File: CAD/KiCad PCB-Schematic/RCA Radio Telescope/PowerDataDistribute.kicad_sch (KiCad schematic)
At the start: 12 parts, among them J7 USB_A, J8 USB_A, Q1 PMOS, U13 MIC23050-SYML-TR

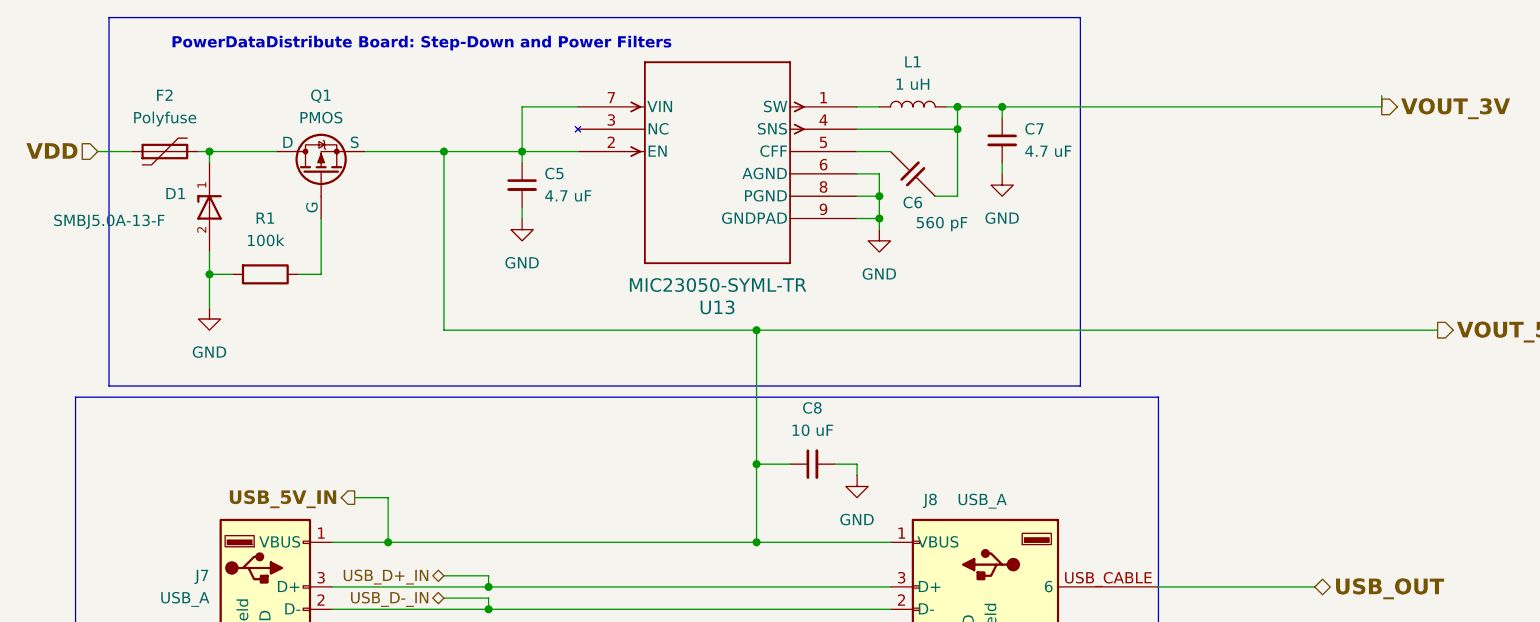
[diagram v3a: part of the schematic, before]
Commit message: Updated PowerDataDistribute schematicto v1.4
- Added components for fuses and PMOS
- Created PCB v1.0
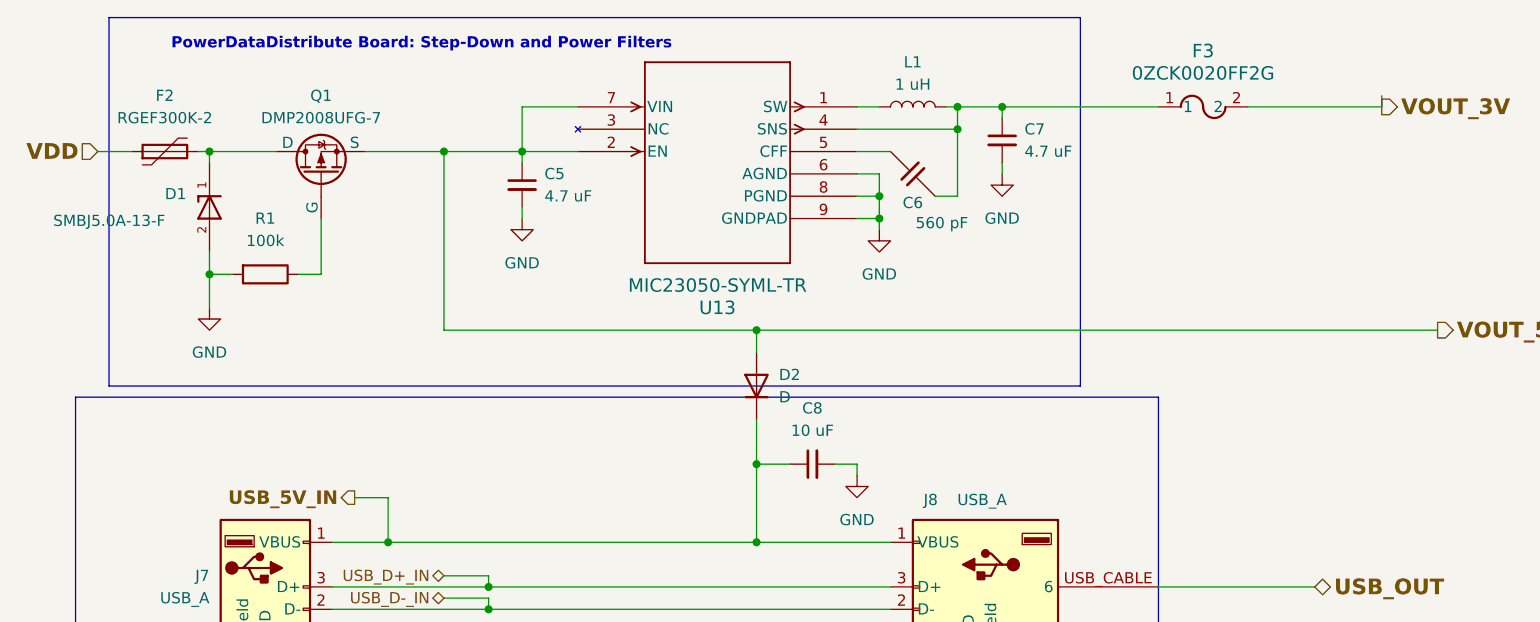
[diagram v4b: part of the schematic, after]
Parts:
- added D2: D, Diode_SMD:D_0805_2012Metric, symbol Device:D
- added F3: 0ZCK0020FF2G, Library:0ZCK_BEL, symbol Radio Telescope:0ZCK0020FF2G
- C5, C6, C7, C8: footprint (none) -> Capacitor_SMD:C_0805_2012Metric
- F2: value Polyfuse -> RGEF300K-2; footprint (none) -> Library:RGEF300K-2
- J7, J8: footprint (none) -> Library:CONN_AU-Y1005-2_ASM
- L1: footprint (none) -> Inductor_SMD:L_0805_2012Metric
- Q1: value PMOS -> DMP2008UFG-7; footprint (none) -> Library:DMP2008UFG-7_DIO
- R1: footprint (none) -> Resistor_SMD:R_0805_2012Metric
- U13: footprint MLF-8_ML_MCH -> Library:MLF-8_ML_MCH
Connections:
- net USB_5V_IN: now also D2.1 (K); no longer C5.1, Q1.3 (S), U13.2 (EN), U13.7 (VIN)
- net VOUT_3V: now also F3.2; no longer C6.1, C7.1, L1.2, U13.4 (SNS)
- new net: C6.1, C7.1, F3.1, L1.2, U13.4 (SNS)
- new net VOUT_5V: C5.1, D2.2 (A), Q1.3 (S), U13.2 (EN), U13.7 (VIN)
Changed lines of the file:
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@@
 	(title_block
 		(title "PowerDataDistribute")
-		(rev "Version 1.3")
+		(date "2025-03-15")
+		(rev "Version 1.4")
 	)
 	(junction
@@
 	)
 	(junction
+		(at 123.19 25.4)
+		(diameter 0)
+		(color 0 0 0 0)
+	)
+	(junction
 		(at 53.34 74.93)
 		(diameter 0)
@@
 	)
 	(junction
-		(at 123.19 25.4)
-		(diameter 0)
-		(color 0 0 0 0)
-	)
-	(junction
 		(at 118.11 27.94)
 		(diameter 0)
@@
 	(wire
 		(pts
+			(xy 95.25 60.96) (xy 95.25 66.04)
+		)
+		(stroke
+			(width 0)
+			(type default)
+		)
+	)
+	(wire
+		(pts
 			(xy 109.22 38.1) (xy 109.22 39.37)
 		)
@@
 	(wire
 		(pts
+			(xy 151.13 25.4) (xy 166.37 25.4)
+		)
+		(stroke
+			(width 0)
+			(type default)
+		)
+	)
+	(wire
+		(pts
 			(xy 104.14 66.04) (xy 106.68 66.04)
 		)
@@
 	(wire
 		(pts
+			(xy 123.19 25.4) (xy 140.97 25.4)
+		)
+		(stroke
+			(width 0)
+			(type default)
+		)
+	)
+	(wire
+		(pts
 			(xy 33.02 44.45) (xy 35.56 44.45)
 		)
@@
 	(wire
 		(pts
-			(xy 123.19 25.4) (xy 166.37 25.4)
-		)
-		(stroke
-			(width 0)
-			(type default)
-		)
-	)
-	(wire
-		(pts
 			(xy 106.68 35.56) (xy 109.22 35.56)
 		)
@@
 	(wire
 		(pts
-			(xy 95.25 50.8) (xy 95.25 66.04)
+			(xy 95.25 50.8) (xy 95.25 53.34)
 		)
 		(stroke
@@
 			)
 		)
-		(property "Value" "Polyfuse"
+		(property "Value" "RGEF300K-2"
 			(at 27.94 26.67 90)
 			(effects
@@
 			)
 		)
-		(property "Footprint" ""
+		(property "Footprint" "Library:RGEF300K-2"
 			(at 33.02 29.21 0)
 			(effects
@@
 			)
 		)
-		(property "Footprint" ""
+		(property "Footprint" "Capacitor_SMD:C_0805_2012Metric"
 			(at 113.03 31.242 0)
 			(effects
@@
 			)
 		)
-		(property "Footprint" "MLF-8_ML_MCH"
+		(property "Footprint" "Library:MLF-8_ML_MCH"
 			(at 72.39 51.308 0)
 			(effects
@@
 			)
 		)
-		(property "Footprint" ""
+		(property "Footprint" "Library:CONN_AU-Y1005-2_ASM"
 			(at 124.46 69.85 0)
 			(effects
@@
 			)
 		)
-		(property "Value" "PMOS"
+		(property "Value" "DMP2008UFG-7"
 			(at 45.72 26.67 90)
 			(effects
@@
 			)
 		)
-		(property "Footprint" ""
+		(property "Footprint" "Library:DMP2008UFG-7_DIO"
 			(at 43.18 27.94 0)
 			(effects
@@
 			)
 		)
-		(property "Footprint" ""
+		(property "Footprint" "Capacitor_SMD:C_0805_2012Metric"
 			(at 68.58 34.29 0)
 			(effects
@@
 				(path "/1630c5ee-b70a-455e-85ba-86a73955b8fd/27e6aa46-cfac-490f-80c1-5c0f7cb6c2e8"
 					(reference "C5")
+					(unit 1)
+				)
+			)
+		)
+	)
+	(symbol
+		(lib_id "Device:D")
+		(at 95.25 57.15 90)
+		(unit 1)
+		(exclude_from_sim no)
+		(in_bom yes)
+		(on_board yes)
+		(dnp no)
+		(fields_autoplaced yes)
+		(property "Reference" "D2"
+			(at 97.79 55.8799 90)
+			(effects
+				(font
+					(size 1.27 1.27)
+				)
+				(justify right)
+			)
+		)
+		(property "Value" "D"
+			(at 97.79 58.4199 90)
+			(effects
+				(font
+					(size 1.27 1.27)
+				)
+				(justify right)
+			)
+		)
+		(property "Footprint" "Diode_SMD:D_0805_2012Metric"
+			(at 95.25 57.15 0)
+			(effects
+				(font
+					(size 1.27 1.27)
+				)
+				(hide yes)
+			)
+		)
+		(property "Datasheet" "~"
+			(at 95.25 57.15 0)
+			(effects
+				(font
+					(size 1.27 1.27)
+				)
+				(hide yes)
+			)
+		)
+		(property "Description" "Diode"
+			(at 95.25 57.15 0)
+			(effects
+				(font
+					(size 1.27 1.27)
+				)
+				(hide yes)
+			)
+		)
+		(property "Sim.Device" "D"
+			(at 95.25 57.15 0)
+			(effects
+				(font
+					(size 1.27 1.27)
+				)
+				(hide yes)
+			)
+		)
+		(property "Sim.Pins" "1=K 2=A"
+			(at 95.25 57.15 0)
+			(effects
+				(font
+					(size 1.27 1.27)
+				)
+				(hide yes)
+			)
+		)
+		(pin "2"
+		)
+		(pin "1"
+		)
+		(instances
+			(project ""
+				(path "/1630c5ee-b70a-455e-85ba-86a73955b8fd/27e6aa46-cfac-490f-80c1-5c0f7cb6c2e8"
+					(reference "D2")
 					(unit 1)
 				)
@@
 			)
 		)
-		(property "Footprint" ""
+		(property "Footprint" "Resistor_SMD:R_0805_2012Metric"
 			(at 39.37 42.672 90)
 			(effects
@@
 				(path "/1630c5ee-b70a-455e-85ba-86a73955b8fd/27e6aa46-cfac-490f-80c1-5c0f7cb6c2e8"
 					(reference "R1")
+					(unit 1)
+				)
+			)
+		)
+	)
+	(symbol
+		(lib_id "Radio Telescope:0ZCK0020FF2G")
+		(at 140.97 25.4 0)
+		(unit 1)
+		(exclude_from_sim no)
+		(in_bom yes)
+		(on_board yes)
+		(dnp no)
+		(fields_autoplaced yes)
+		(property "Reference" "F3"
+			(at 146.05 19.05 0)
+			(effects
+				(font
+					(size 1.524 1.524)
+				)
+			)
+		)
+		(property "Value" "0ZCK0020FF2G"
+			(at 146.05 21.59 0)
+			(effects
+				(font
+					(size 1.524 1.524)
+				)
+			)
+		)
+		(property "Footprint" "Library:0ZCK_BEL"
+			(at 138.938 19.558 0)
+			(effects
+				(font
+					(size 1.27 1.27)
+					(italic yes)
+				)
+				(hide yes)
+			)
+		)
+		(property "Datasheet" "0ZCK0020FF2G"
+			(at 137.668 16.51 0)
+			(effects
+				(font
+					(size 1.27 1.27)
+					(italic yes)
+				)
+				(hide yes)
+			)
+		)
+		(property "Description" ""
+			(at 140.97 25.4 0)
+			(effects
+				(font
+					(size 1.27 1.27)
+				)
+				(hide yes)
+			)
+		)
+		(pin "2"
+		)
+		(pin "1"
+		)
+		(instances
+			(project ""
+				(path "/1630c5ee-b70a-455e-85ba-86a73955b8fd/27e6aa46-cfac-490f-80c1-5c0f7cb6c2e8"
+					(reference "F3")
 					(unit 1)
 				)
@@
 			)
 		)
-		(property "Footprint" ""
+		(property "Footprint" "Capacitor_SMD:C_0805_2012Metric"
 			(at 123.19 29.21 0)
 			(effects
@@
 			)
 		)
-		(property "Footprint" ""
+		(property "Footprint" "Capacitor_SMD:C_0805_2012Metric"
 			(at 101.6 66.04 0)
 			(effects
@@
 			)
 		)
-		(property "Footprint" ""
+		(property "Footprint" "Library:CONN_AU-Y1005-2_ASM"
 			(at 43.18 81.28 0)
 			(effects
@@
 			)
 		)
-		(property "Footprint" ""
+		(property "Footprint" "Inductor_SMD:L_0805_2012Metric"
 			(at 113.03 25.4 0)
 			(effects

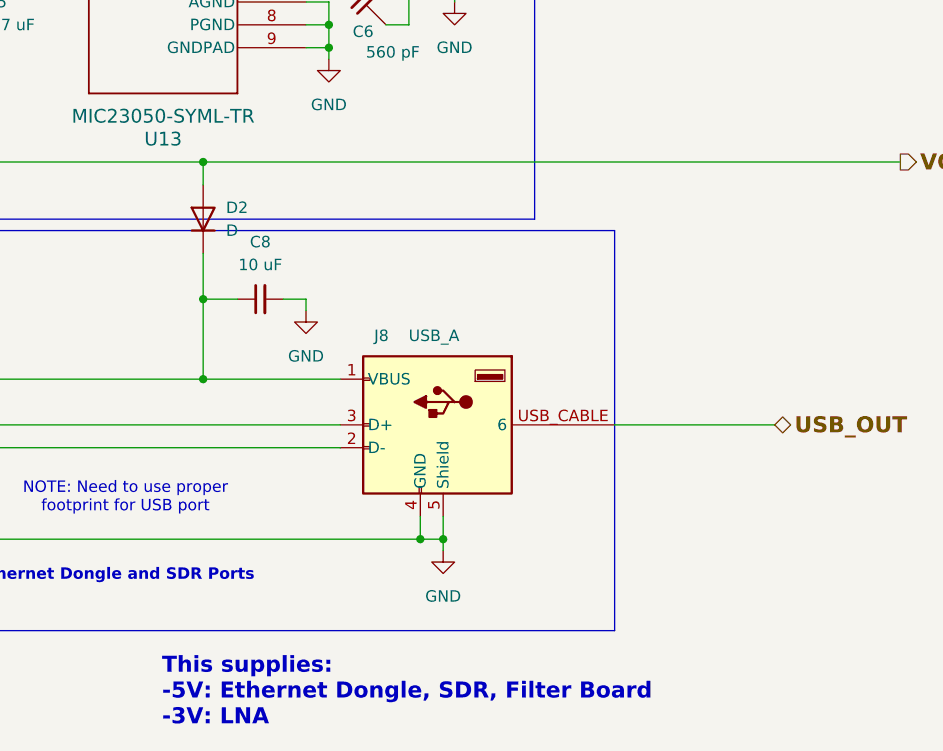
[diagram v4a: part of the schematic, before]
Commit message: Updated PowerData Board to v1.2
- Added zone fills for certain pins
- Added ground vias for mounting holes
- Minor readjustments to components
- Added silkscreen for voltage polarity
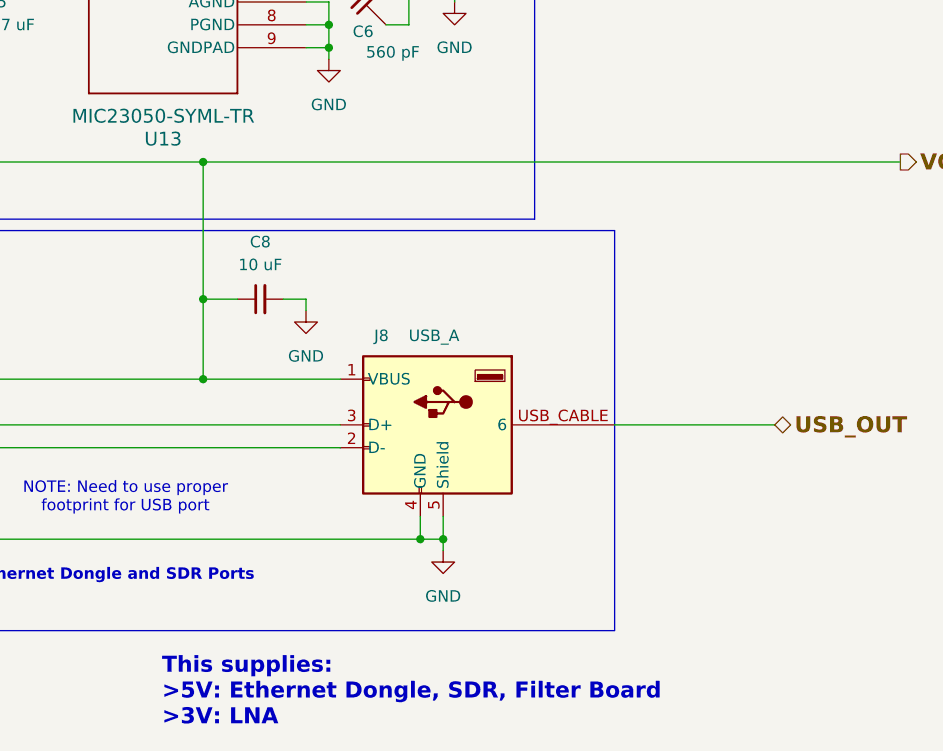
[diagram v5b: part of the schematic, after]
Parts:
- removed D2: D, Diode_SMD:D_0805_2012Metric, symbol Device:D
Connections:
- net VOUT_5V is gone; now on net USB_5V_IN: C5.1, Q1.3 (S), U13.2 (EN), U13.7 (VIN)
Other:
- note added: "This supplies: >5V: Ethernet Dongle, SDR, Filter Board >3V: LNA"
- note removed: "This supplies: -5V: Ethernet Dongle, SDR, Filter Board -3V: LNA"
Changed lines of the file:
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@@
-	(wire
-		(pts
-			(xy 95.25 60.96) (xy 95.25 66.04)
-		)
-		(stroke
-			(width 0)
-			(type default)
-		)
-	)
 	(wire
 		(pts
@@
 	(wire
 		(pts
-			(xy 95.25 50.8) (xy 95.25 53.34)
+			(xy 95.25 50.8) (xy 95.25 66.04)
 		)
 		(stroke
@@
 		)
 	)
-	(text "This supplies:\n-5V: Ethernet Dongle, SDR, Filter Board\n-3V: LNA"
+	(text "This supplies:\n>5V: Ethernet Dongle, SDR, Filter Board\n>3V: LNA"
 		(exclude_from_sim no)
 		(at 90.678 109.728 0)
@@
 					(unit 1)
 				)
-			)
-		)
-	)
-	(symbol
-		(lib_id "Device:D")
-		(at 95.25 57.15 90)
-		(unit 1)
-		(exclude_from_sim no)
-		(in_bom yes)
-		(on_board yes)
-		(dnp no)
-		(fields_autoplaced yes)
-		(property "Reference" "D2"
-			(at 97.79 55.8799 90)
-			(effects
-				(font
-					(size 1.27 1.27)
-				)
-				(justify right)
-			)
-		)
-		(property "Value" "D"
-			(at 97.79 58.4199 90)
-			(effects
-				(font
-					(size 1.27 1.27)
-				)
-				(justify right)
-			)
-		)
-		(property "Footprint" "Diode_SMD:D_0805_2012Metric"
-			(at 95.25 57.15 0)
-			(effects
-				(font
-					(size 1.27 1.27)
-				)
-				(hide yes)
-			)
-		)
-		(property "Datasheet" "~"
-			(at 95.25 57.15 0)
-			(effects
-				(font
-					(size 1.27 1.27)
-				)
-				(hide yes)
-			)
-		)
-		(property "Description" "Diode"
-			(at 95.25 57.15 0)
-			(effects
-				(font
-					(size 1.27 1.27)
-				)
-				(hide yes)
-			)
-		)
-		(property "Sim.Device" "D"
-			(at 95.25 57.15 0)
-			(effects
-				(font
-					(size 1.27 1.27)
-				)
-				(hide yes)
-			)
-		)
-		(property "Sim.Pins" "1=K 2=A"
-			(at 95.25 57.15 0)
-			(effects
-				(font
-					(size 1.27 1.27)
-				)
-				(hide yes)
-			)
-		)
-		(pin "2"
-		)
-		(pin "1"
-		)
-		(instances
-			(project ""
-				(path "/1630c5ee-b70a-455e-85ba-86a73955b8fd/27e6aa46-cfac-490f-80c1-5c0f7cb6c2e8"
-					(reference "D2")
-					(unit 1)
-				)

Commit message: V1.5 Schematic and 1.4 PCB Layout
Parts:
- added C10: 0.1uF, Capacitor_SMD:C_0805_2012Metric, symbol Device:C_Small
- added C11: 3.3nF, Capacitor_SMD:C_0805_2012Metric, symbol Device:C_Small
- added C12: 22uF, Capacitor_SMD:C_0805_2012Metric, symbol Device:C_Small
- added C9: 10uF, Capacitor_SMD:C_0805_2012Metric, symbol Device:C_Small
- added L2: 2.2uH, Inductor_SMD:L_0805_2012Metric, symbol Device:L
- added R2: 100k, Resistor_SMD:R_0805_2012Metric, symbol Device:R_Small
- added U14: TPS62133RGTR, TPS62133RGTR:RGT0016C, symbol TPS62133RGTR:TPS62133RGTR
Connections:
- net GND: now also C10.2, C11.1, C12.2, C9.2, U14.15 (PGND), U14.16 (PGND), U14.17 (EP), U14.5 (FB), U14.6 (AGND), U14.7 (FSW), U14.8 (DEF)
- net USB_5V_IN: now also C12.1, L2.2, R2.1, U14.14 (VOS); no longer Q1.3 (S)
- new net: L2.1, U14.1 (SW), U14.2 (SW), U14.3 (SW)
- new net: C10.1, C9.1, Q1.3 (S), U14.10 (AVIN), U14.11 (PVIN), U14.12 (PVIN), U14.13 (EN)
- new net: R2.2, U14.4 (PG)
- new net: C11.2, U14.9 (SS_TR)
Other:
- moved on the sheet: C5, C6, C7, C8, F3, J7, J8, L1, U13
